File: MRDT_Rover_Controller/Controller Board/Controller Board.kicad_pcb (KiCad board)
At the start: 2 copper layers, 137.6 x 81.5 mm, 30 parts, among them Q1 S8050, SW1 EG1218, U1 MCP3008

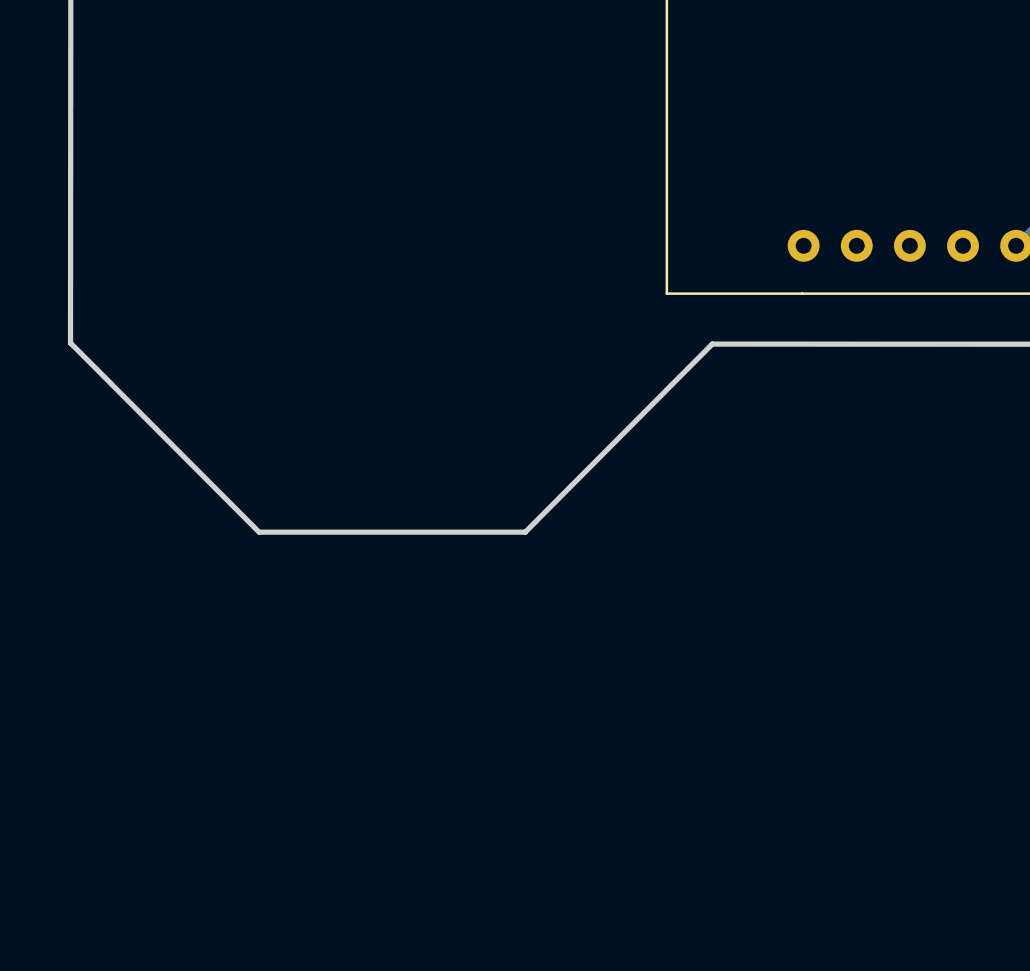
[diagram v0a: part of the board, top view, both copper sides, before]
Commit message: MRDT Silkscreen added
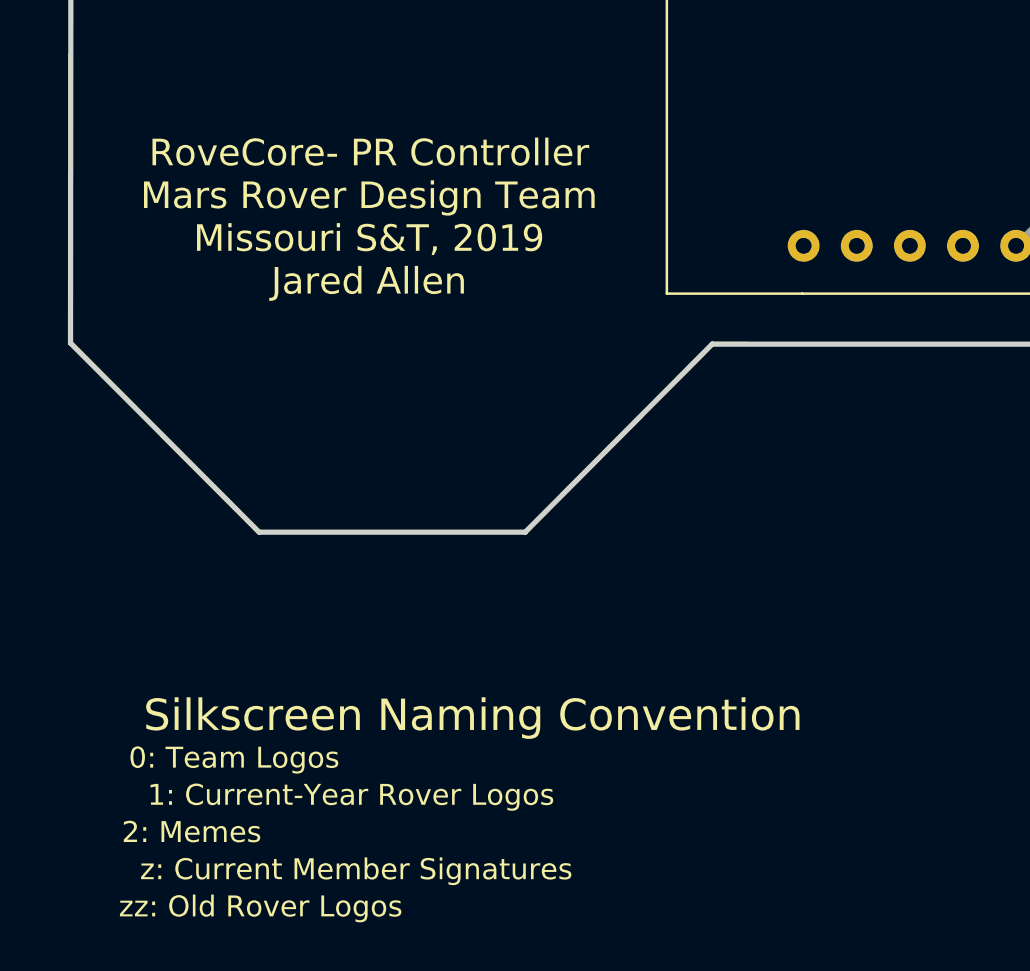
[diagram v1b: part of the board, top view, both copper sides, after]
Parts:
- added G***: LOGO, MRDT_Silkscreens:0-README, F.Cu at (88.5, 147.6)
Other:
- board text added: "RoveCore- PR Controller Mars Rover Design Team Missouri S&T, 2019 Jared Allen"
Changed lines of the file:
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@@
   (general
     (thickness 1.6)
-    (drawings 25)
+    (drawings 26)
     (tracks 605)
     (zones 0)
-    (modules 30)
+    (modules 31)
     (nets 69)
   )
@@
   )
   (setup
-    (last_trace_width 0.381)
+    (last_trace_width 0.25)
     (user_trace_width 0.381)
     (user_trace_width 15)
@@
     (add_net V0)
   )
+  (module MRDT_Silkscreens:0-README (layer F.Cu)
+    (at 88.5444 147.6248)
+    (fp_text reference G*** (at -10.2362 6.0198) (layer Dwgs.User) hide
+      (effects (font (size 0.2 0.2) (thickness 0.05)))
+    )
+    (fp_text value LOGO (at -10.541 -0.7874) (layer Dwgs.User) hide
+      (effects (font (size 0.2 0.2) (thickness 0.05)))
+    )
+    (fp_text user "Silkscreen Naming Convention" (at 6.604 -5.334) (layer F.SilkS)
+      (effects (font (size 1.5 1.5) (thickness 0.15)))
+    )
+    (fp_text user "zz: Old Rover Logos" (at -3.556 3.81) (layer F.SilkS)
+      (effects (font (size 1 1) (thickness 0.15)))
+    )
+    (fp_text user "z: Current Member Signatures" (at 1.016 2.032) (layer F.SilkS)
+      (effects (font (size 1 1) (thickness 0.15)))
+    )
+    (fp_text user "2: Memes" (at -6.858 0.254) (layer F.SilkS)
+      (effects (font (size 1 1) (thickness 0.15)))
+    )
+    (fp_text user "1: Current-Year Rover Logos" (at 0.762 -1.524) (layer F.SilkS)
+      (effects (font (size 1 1) (thickness 0.15)))
+    )
+    (fp_text user "0: Team Logos" (at -4.826 -3.302) (layer F.SilkS)
+      (effects (font (size 1 1) (thickness 0.15)))
+    )
+  )
   (module Display:WC1602A (layer F.Cu)
     (at 113.03 55.88)
@@
     )
   )
+  (gr_text "RoveCore- PR Controller\nMars Rover Design Team\nMissouri S&T, 2019\nJared Allen" (at 90.17 118.4656) (layer F.SilkS)
+    (effects (font (size 1.27 1.27) (thickness 0.2032)))
+  )
   (gr_line (start 97.6376 133.5278) (end 106.5784 124.5362) (layer Edge.Cuts) (width 0.25))

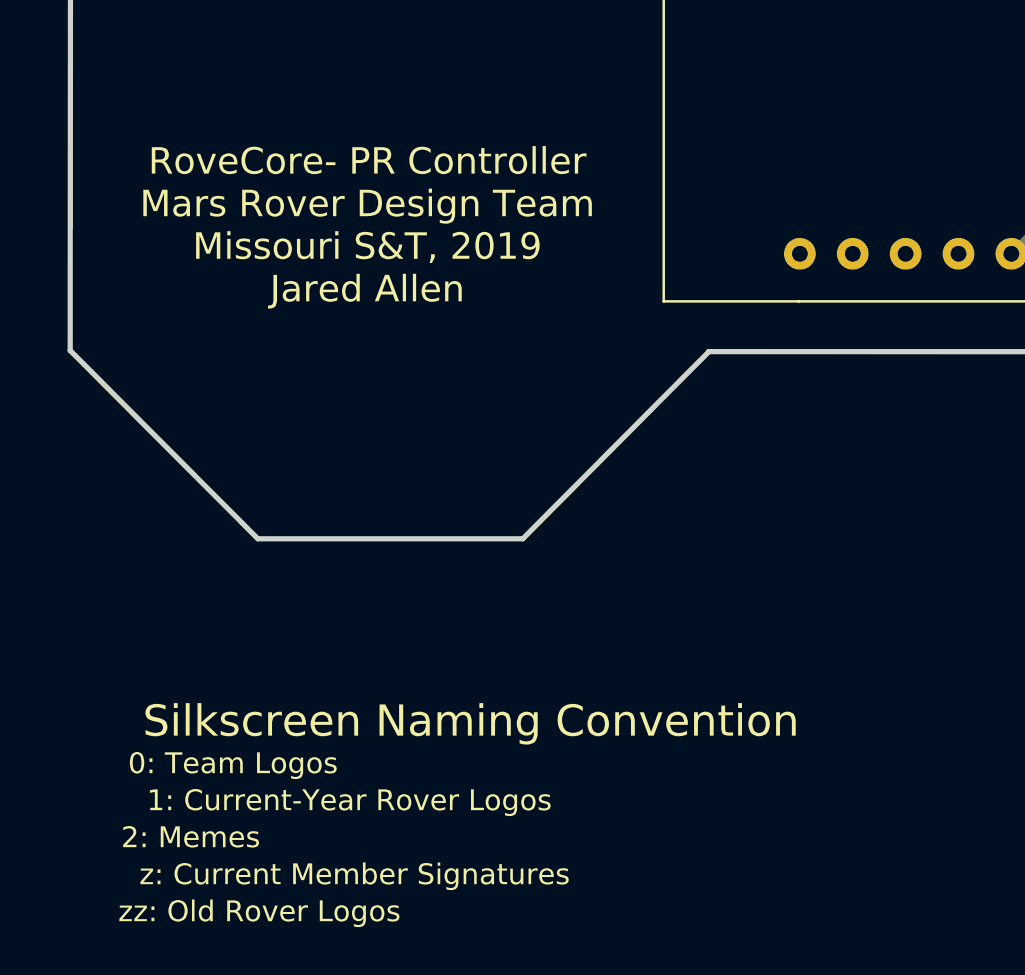
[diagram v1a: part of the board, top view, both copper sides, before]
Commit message: Silkscreen Updated with MRDT Logo
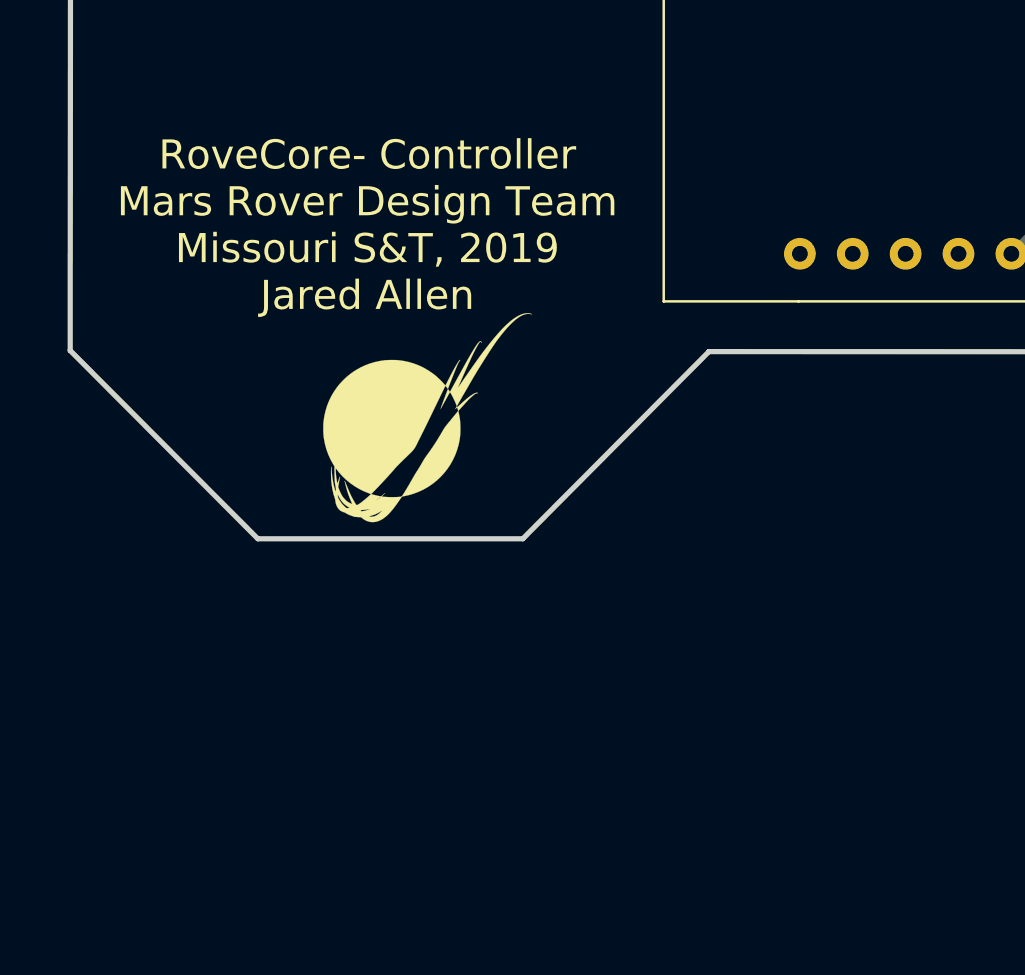
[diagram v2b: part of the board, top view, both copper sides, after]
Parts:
- removed the G*** at (88.5, 147.6)
- added G***: LOGO, MRDT_Silkscreens:0_MRDT_Logo_10mm, F.Cu at (93.1, 127.7)
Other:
- board text added: "RoveCore- Controller Mars Rover Design Team Missouri S&T, 2019 Jared Allen"
- board text removed: "RoveCore- PR Controller Mars Rover Design Team Missouri S&T, 2019 Jared Allen"

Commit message: Symbol Updates
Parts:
- moved BAT1 0.05 mm to (156.2, 86.6)
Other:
- board text added: "RoveCore- Controller Mars Rover Design Team Missouri S&T, 2020 Jared Allen"
- board text removed: "RoveCore- Controller Mars Rover Design Team Missouri S&T, 2019 Jared Allen"
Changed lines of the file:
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@@
   )
   (module digikey-footprints:Battery_Holder_9V_BC9VPC-ND (layer B.Cu)
-    (at 156.21 86.614)
+    (at 156.21 86.5632)
     (descr http://www.memoryprotectiondevices.com/datasheets/BC9VPC-datasheet.pdf)
     (fp_text reference BAT1 (at -12.54 4.91 180) (layer B.SilkS)
@@
     )
   )
-  (gr_text "RoveCore- Controller\nMars Rover Design Team\nMissouri S&T, 2019\nJared Allen" (at 90.17 118.4656) (layer F.SilkS)
+  (gr_text "RoveCore- Controller\nMars Rover Design Team\nMissouri S&T, 2020\nJared Allen" (at 90.17 118.4656) (layer F.SilkS)
     (effects (font (size 1.397 1.397) (thickness 0.2032)))
   )

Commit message: Silkscreen Updated
Capactior connections made with new capactior at input of 7805, and silkscreen updated.
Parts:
- removed G***: LOGO, MRDT_Silkscreens:0_MRDT_Logo_10mm
- added C2: 1uF, Capacitor_SMD:C_0603_1608Metric_Pad1.05x0.95mm_HandSolder, F.Cu at (210.8, 63.5)
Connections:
- 5V_Regulator1 pad 2: GND -> Net-(5V_Regulator1-Pad2)
- SW1 pad 1: Net-(5V_Regulator1-Pad1) -> Net-(C2-Pad2)
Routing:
- net Net-(C2-Pad2): track 0.00 -> 25.2 mm
- net Net-(5V_Regulator1-Pad1): track 21.1 -> 25.3 mm, vias 0 -> 1
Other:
- board text added: "OFF"
- board text added: "ON"
- board text added: "SafeDrive"
- board text added: "TankDrive"

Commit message: Silkscreen Updated
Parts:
- renumbered LED2 to COM, LED1 to PWR
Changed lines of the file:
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@@
   (module MRDT_Actives:LED_CREE_XLAMP_XPG (layer F.Cu)
     (at 92.71 59.69)
-    (fp_text reference LED2 (at 0.127 2.413) (layer F.SilkS)
+    (fp_text reference COM (at 0.127 2.413) (layer F.SilkS)
       (effects (font (size 0.6 0.6) (thickness 0.15)))
     )
@@
   (module MRDT_Actives:LED_CREE_XLAMP_XPG (layer F.Cu)
     (at 85.09 59.69)
-    (fp_text reference LED1 (at 0.127 2.413) (layer F.SilkS)
+    (fp_text reference PWR (at 0.127 2.413) (layer F.SilkS)
       (effects (font (size 0.6 0.6) (thickness 0.15)))
     )

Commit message: 7805 Input Capacitor Updated
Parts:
- renumbered PWR to LED1, COM to LED2
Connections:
- C2 pad 1: Net-(5V_Regulator1-Pad1) -> GND
- C2 pad 2: Net-(C2-Pad2) -> Net-(5V_Regulator1-Pad1)
- SW1 pad 1: Net-(C2-Pad2) -> Net-(5V_Regulator1-Pad1)
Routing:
- net Net-(C2-Pad2): track 25.2 -> 0.00 mm
- net Net-(5V_Regulator1-Pad1): track 25.3 -> 46.3 mm, vias 1 -> 0
- net GND: track 440.2 -> 441.8 mm
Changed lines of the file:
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@@
     (thickness 1.6)
     (drawings 30)
-    (tracks 618)
+    (tracks 619)
     (zones 0)
     (modules 31)
-    (nets 71)
+    (nets 70)
   )
   (page A4)
@@
   (net 68 "Net-(SW1-Pad3)")
   (net 69 "Net-(5V_Regulator1-Pad2)")
-  (net 70 "Net-(C2-Pad2)")
   (net_class Default "This is the default net class."
     (clearance 0.2)
@@
     (add_net "Net-(5V_Regulator1-Pad2)")
     (add_net "Net-(BAT1-PadPOS)")
-    (add_net "Net-(C2-Pad2)")
     (add_net "Net-(ESP-12E1-Pad1)")
     (add_net "Net-(ESP-12E1-Pad12)")
@@
       (net 67 "Net-(BAT1-PadPOS)"))
     (pad 1 thru_hole rect (at 0 0) (size 1.9 1.9) (drill 0.9) (layers *.Cu *.Mask)
-      (net 70 "Net-(C2-Pad2)"))
+      (net 15 "Net-(5V_Regulator1-Pad1)"))
     (model "B:/GitHub/RemoteController_Hardware/3D Models/EG1218.stp"
       (offset (xyz 2.5 0 0))
@@
   (module MRDT_Actives:LED_CREE_XLAMP_XPG (layer F.Cu)
     (at 92.71 59.69)
-    (fp_text reference COM (at 0.127 2.413) (layer F.SilkS)
+    (fp_text reference LED2 (at 0.127 2.413) (layer F.SilkS)
       (effects (font (size 0.6 0.6) (thickness 0.15)))
     )
@@
   (module MRDT_Actives:LED_CREE_XLAMP_XPG (layer F.Cu)
     (at 85.09 59.69)
-    (fp_text reference PWR (at 0.127 2.413) (layer F.SilkS)
+    (fp_text reference LED1 (at 0.127 2.413) (layer F.SilkS)
       (effects (font (size 0.6 0.6) (thickness 0.15)))
     )
@@
     )
     (pad 1 smd roundrect (at -0.875 0 90) (size 1.05 0.95) (layers F.Cu F.Paste F.Mask) (roundrect_rratio 0.25)
+      (net 14 GND))
+    (pad 2 smd roundrect (at 0.875 0 90) (size 1.05 0.95) (layers F.Cu F.Paste F.Mask) (roundrect_rratio 0.25)
       (net 15 "Net-(5V_Regulator1-Pad1)"))
-    (pad 2 smd roundrect (at 0.875 0 90) (size 1.05 0.95) (layers F.Cu F.Paste F.Mask) (roundrect_rratio 0.25)
-      (net 70 "Net-(C2-Pad2)"))
     (model ${KISYS3DMOD}/Capacitor_SMD.3dshapes/C_0603_1608Metric.wrl
       (at (xyz 0 0 0))
@@
   (gr_line (start 106.589744 124.550256) (end 97.609488 133.530512) (layer Dwgs.User) (width 0.2))
   (gr_line (start 204.47 52.07) (end 84.909488 52.07) (layer Dwgs.User) (width 0.2))
-  (via (at 210.7184 64.4652) (size 0.8) (drill 0.4) (layers F.Cu B.Cu) (net 15))
   (segment (start 181.7624 118.2998) (end 177.3428 113.8802) (width 0.381) (layer B.Cu) (net 1))
   (segment (start 181.7624 119.4308) (end 181.7624 118.2998) (width 0.381) (layer B.Cu) (net 1))
@@
   (segment (start 184.658 66.04) (end 202.581 66.04) (width 0.381) (layer B.Cu) (net 14))
   (segment (start 207.494 62.992) (end 207.01 62.992) (width 0.381) (layer F.Cu) (net 14))
-  (segment (start 210.82 66.318) (end 207.494 62.992) (width 0.381) (layer F.Cu) (net 14))
   (segment (start 210.82 66.943) (end 210.82 66.9036) (width 0.381) (layer F.Cu) (net 14))
   (segment (start 195.961 100.203) (end 195.961 97.028) (width 0.381) (layer B.Cu) (net 14))
@@
   (segment (start 92.71 96.278765) (end 86.995 90.563765) (width 0.381) (layer F.Cu) (net 14))
   (segment (start 92.71 97.536) (end 92.71 96.278765) (width 0.381) (layer F.Cu) (net 14))
+  (segment (start 210.270128 65.768128) (end 210.2746 65.7726) (width 0.25) (layer F.Cu) (net 14))
+  (segment (start 210.270128 64.913472) (end 210.270128 65.768128) (width 0.25) (layer F.Cu) (net 14))
+  (segment (start 210.7692 64.4144) (end 210.270128 64.913472) (width 0.25) (layer F.Cu) (net 14))
+  (segment (start 210.82 66.318) (end 210.2746 65.7726) (width 0.381) (layer F.Cu) (net 14))
+  (segment (start 210.2746 65.7726) (end 207.494 62.992) (width 0.381) (layer F.Cu) (net 14))
   (segment (start 205.629 65.532) (end 198.517 58.42) (width 0.381) (layer F.Cu) (net 15))
   (segment (start 207.01 65.532) (end 205.629 65.532) (width 0.381) (layer F.Cu) (net 15))
@@
   (segment (start 192.8774 58.42) (end 190.9572 56.4998) (width 0.381) (layer F.Cu) (net 15))
   (segment (start 198.517 58.42) (end 192.8774 58.42) (width 0.381) (layer F.Cu) (net 15))
-  (segment (start 209.6516 65.532) (end 207.01 65.532) (width 0.25) (layer B.Cu) (net 15))
-  (segment (start 210.7184 64.4652) (end 209.6516 65.532) (width 0.25) (layer B.Cu) (net 15))
   (segment (start 167.132 109.2708) (end 163.2204 113.1824) (width 0.381) (layer F.Cu) (net 22))
   (segment (start 163.2204 113.1824) (end 163.2204 116.9416) (width 0.381) (layer F.Cu) (net 22))
@@
   (segment (start 192.532 53.3908) (end 189.6364 53.3908) (width 0.381) (layer F.Cu) (net 67))
   (segment (start 189.6364 53.3908) (end 186.683599 56.343601) (width 0.381) (layer F.Cu) (net 67))
-  (segment (start 210.7692 62.6644) (end 210.7692 60.5536) (width 0.25) (layer F.Cu) (net 70))
-  (segment (start 208.12009 57.90449) (end 200.46431 57.90449) (width 0.25) (layer F.Cu) (net 70))
-  (segment (start 210.7692 60.5536) (end 208.12009 57.90449) (width 0.25) (layer F.Cu) (net 70))
-  (segment (start 200.46431 57.90449) (end 199.60822 57.0484) (width 0.25) (layer F.Cu) (net 70))
-  (segment (start 190.743669 54.65329) (end 190.592679 54.80428) (width 0.25) (layer F.Cu) (net 70))
-  (segment (start 191.170731 54.65329) (end 190.743669 54.65329) (width 0.25) (layer F.Cu) (net 70))
-  (segment (start 191.47271 54.955269) (end 191.170731 54.65329) (width 0.25) (layer F.Cu) (net 70))
-  (segment (start 191.47271 55.68431) (end 191.47271 54.955269) (width 0.25) (layer F.Cu) (net 70))
-  (segment (start 199.60822 57.0484) (end 192.8368 57.0484) (width 0.25) (layer F.Cu) (net 70))
-  (segment (start 192.8368 57.0484) (end 191.47271 55.68431) (width 0.25) (layer F.Cu) (net 70))
+  (segment (start 210.7692 62.6644) (end 210.7692 60.5536) (width 0.25) (layer F.Cu) (net 15))
+  (segment (start 208.12009 57.90449) (end 200.46431 57.90449) (width 0.25) (layer F.Cu) (net 15))
+  (segment (start 210.7692 60.5536) (end 208.12009 57.90449) (width 0.25) (layer F.Cu) (net 15))
+  (segment (start 200.46431 57.90449) (end 199.60822 57.0484) (width 0.25) (layer F.Cu) (net 15))
+  (segment (start 190.743669 54.65329) (end 190.592679 54.80428) (width 0.25) (layer F.Cu) (net 15))
+  (segment (start 191.170731 54.65329) (end 190.743669 54.65329) (width 0.25) (layer F.Cu) (net 15))
+  (segment (start 191.47271 54.955269) (end 191.170731 54.65329) (width 0.25) (layer F.Cu) (net 15))
+  (segment (start 191.47271 55.68431) (end 191.47271 54.955269) (width 0.25) (layer F.Cu) (net 15))
+  (segment (start 199.60822 57.0484) (end 192.8368 57.0484) (width 0.25) (layer F.Cu) (net 15))
+  (segment (start 192.8368 57.0484) (end 191.47271 55.68431) (width 0.25) (layer F.Cu) (net 15))
 )
